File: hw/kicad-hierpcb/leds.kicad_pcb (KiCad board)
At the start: 2 copper layers, 8 parts

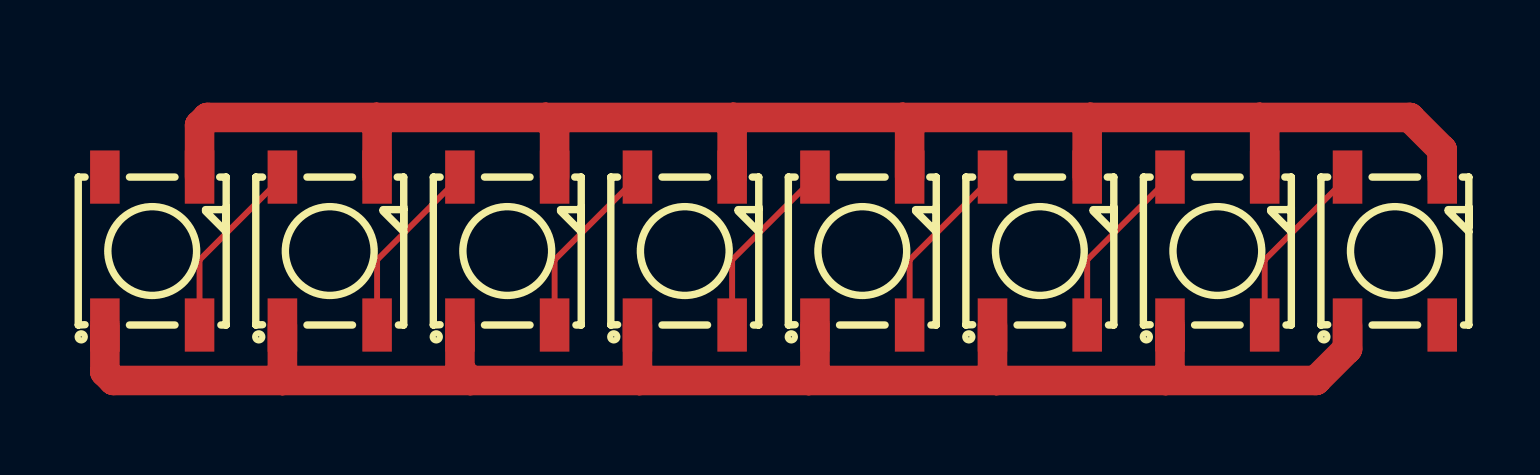
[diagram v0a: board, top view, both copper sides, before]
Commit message: stm32pill pcb
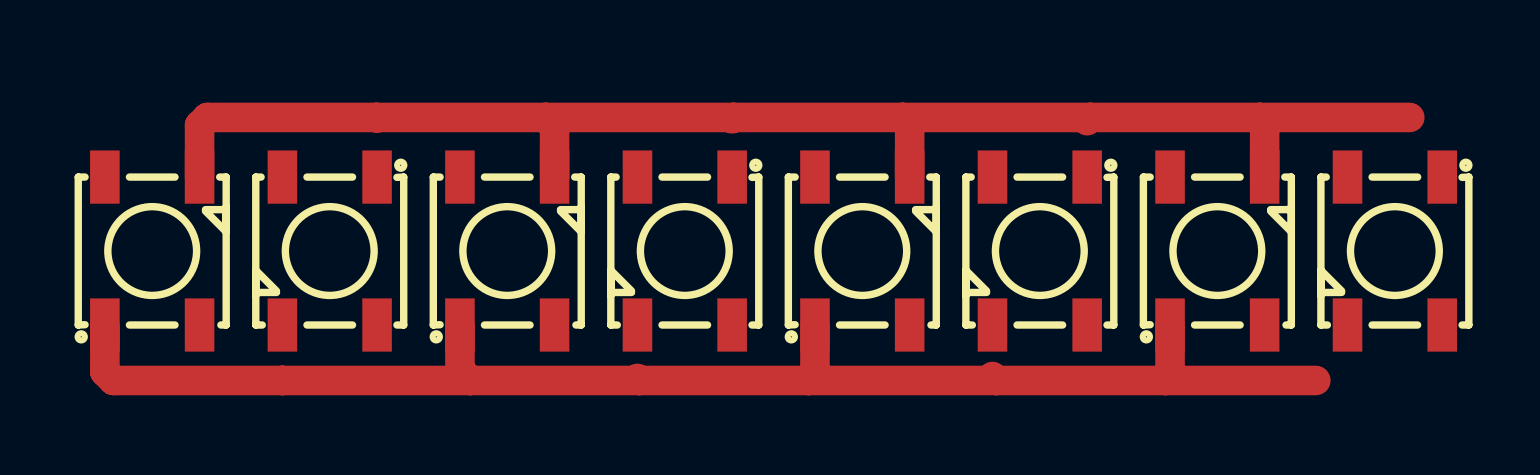
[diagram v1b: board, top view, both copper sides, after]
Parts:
- turned LED2 to -90 degrees
- turned LED4 to -90 degrees
- turned LED6 to -90 degrees
- turned LED8 to -90 degrees
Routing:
- net GND: track 57.7 -> 49.4 mm
- net /VDD: track 56.6 -> 48.9 mm
- net Net-(LED7-DO): track 6.16 -> 0.00 mm
- net Net-(LED6-DO): track 6.16 -> 0.00 mm
- net Net-(LED5-DO): track 6.16 -> 0.00 mm
- net Net-(LED4-DO): track 6.16 -> 0.00 mm
- net Net-(LED3-DO): track 6.16 -> 0.00 mm
- net Net-(LED2-DO): track 6.16 -> 0.00 mm
- net Net-(LED1-DO): track 6.16 -> 0.00 mm

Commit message: stm32-panel
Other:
- board outline added: 48 x 12 mm
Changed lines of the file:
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@@
 		)
+	)
+	(gr_rect
+		(start 129 66)
+		(end 177 78)
+		(stroke
+			(width 0.05)
+			(type default)
+		)
+		(fill none)
+		(layer "Edge.Cuts")
 	)
 	(segment
